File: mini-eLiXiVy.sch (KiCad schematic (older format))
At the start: 175 parts, among them J1 TYPE-C-31-M12_13_EDITED, J2 AVR-ISP-6, SW1 SW_Push, U1 ATmega32U4-AU, U2 WE-TVS-82400102, Y1 Crystal_GND24_Small

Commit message: Added images, adjusted README.md
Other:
- note added: "mini eLiXiVy Schematic, Rev 1a"
- note removed: "mini eLiXiVy Schematic"
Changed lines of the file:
@@
 Text GLabel 7175 1400 1    50   Input ~ 0
 COL13
-Text Notes 2950 750  0    157  ~ 31
-mini eLiXiVy Schematic
+Text Notes 2400 750  0    157  ~ 31
+mini eLiXiVy Schematic, Rev 1a
 $Comp
 L power:GND #PWR0109
@@
 Wire Notes Line
 	7050 6950 7050 8050
-Text Notes 2950 750  0    157  ~ 31
-mini eLiXiVy Schematic
 Text Notes 6670 9892 0    51   ~ 0
 github.com/minibois/eLiXiVy

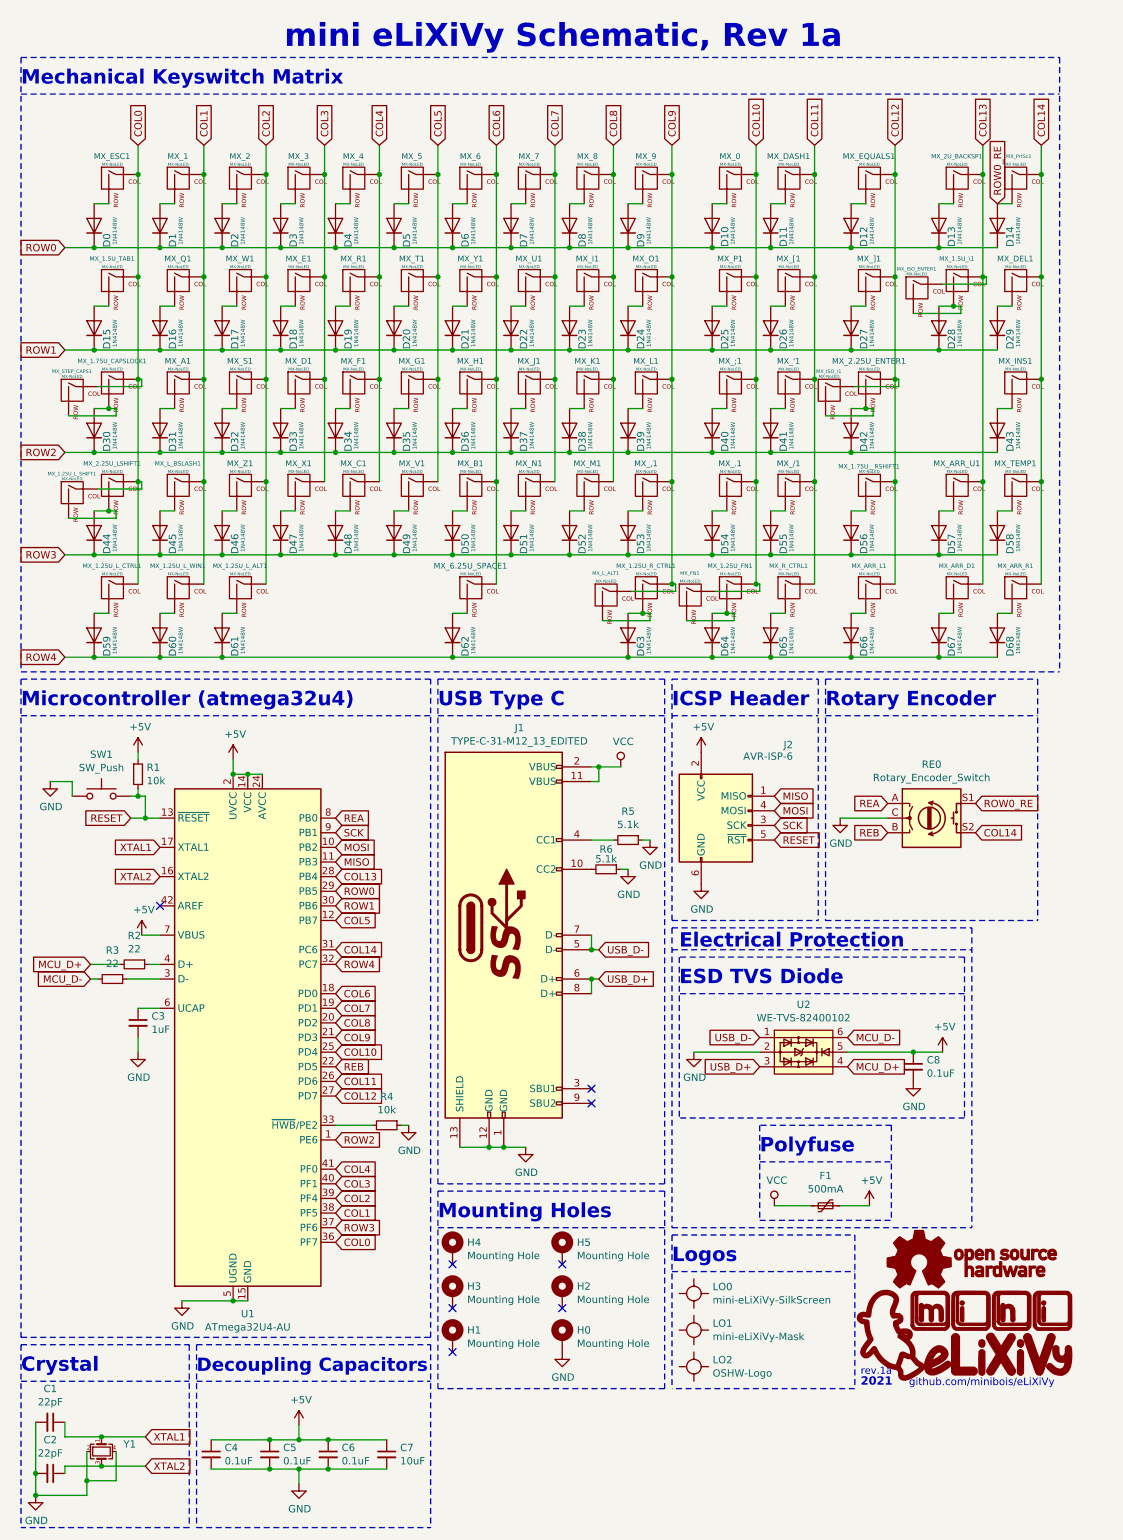
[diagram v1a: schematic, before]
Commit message: rev 1 changes
Changed diode position for D62 and D13 (Spacebar and backspace).
Removed the 'a' from the revision numbers, in the schematic and silkscreen art.
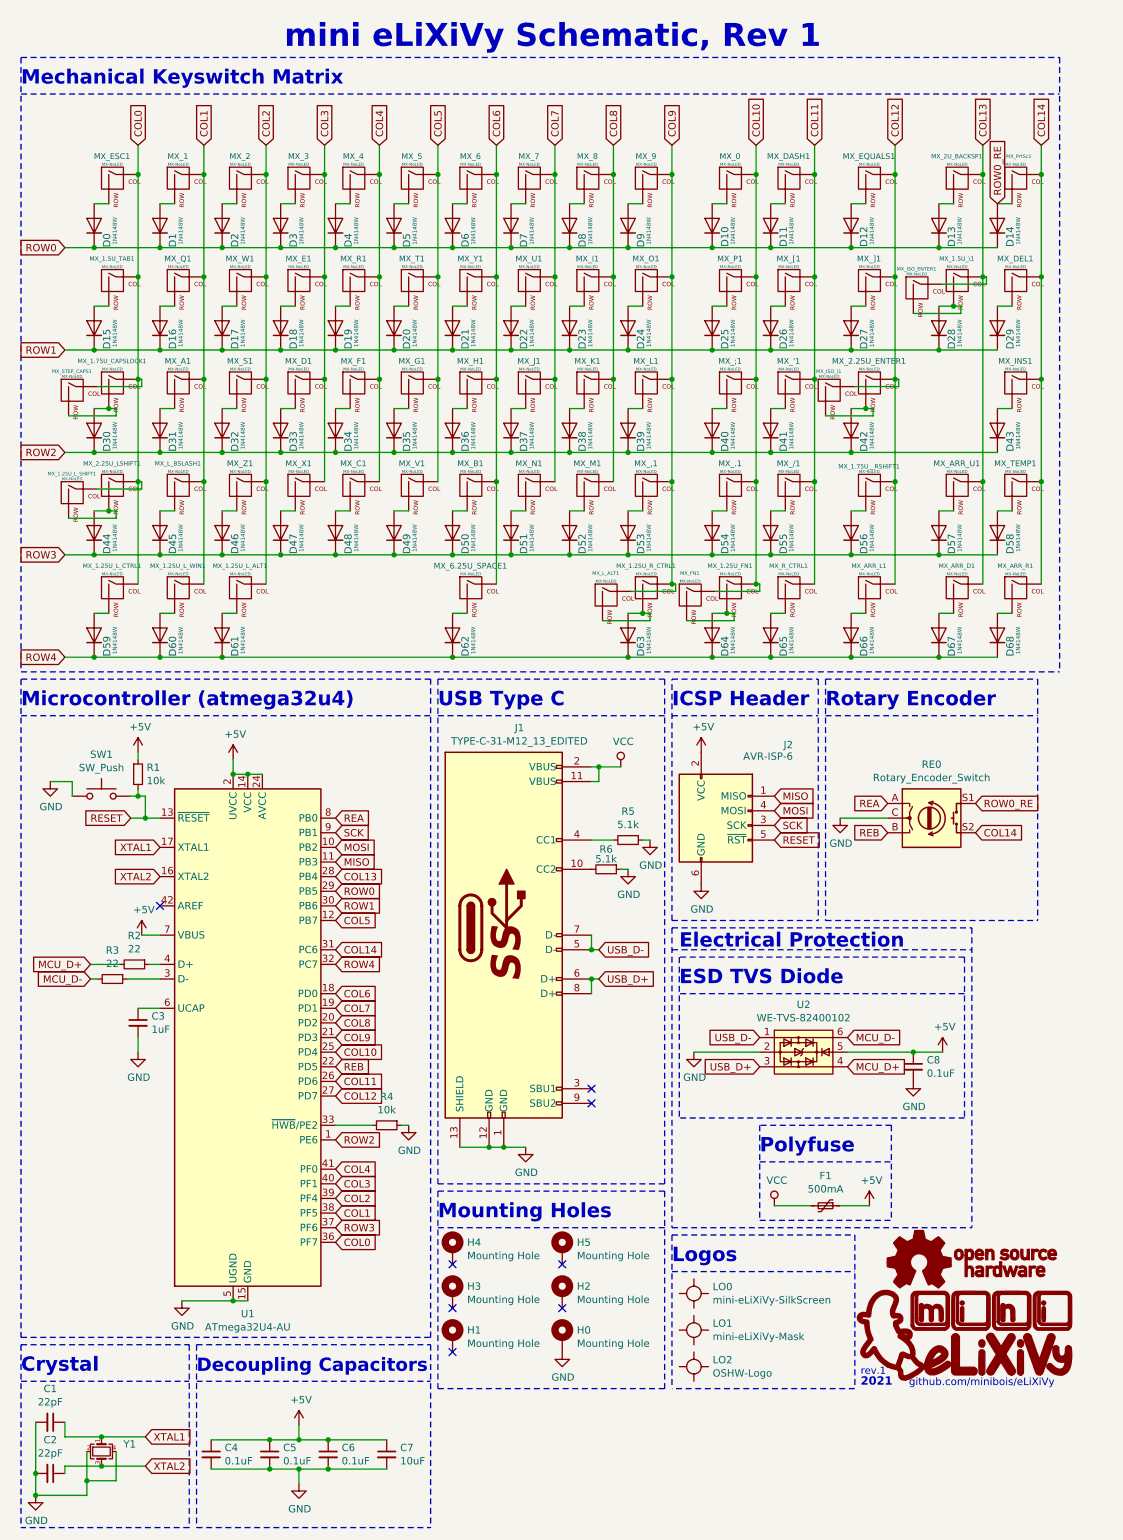
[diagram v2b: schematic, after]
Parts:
- MX_PrtSc1: footprint mini-MX-Tweaks:MXOnly-1U-NoLED-3Pin_tweak -> mini-MX-Tweaks:MXOnly-1U-NoLED_tweak
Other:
- note added: "mini eLiXiVy Schematic, Rev 1"
- note added: "rev.1"
- note removed: "mini eLiXiVy Schematic, Rev 1a"
- note removed: "rev.1a"
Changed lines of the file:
@@
 Sheet 1 1
 Title "eLiXiVy"
-Date "2021-07-09"
-Rev "1a"
+Date "2021-08-05"
+Rev "1"
 Comp "Full License: https://github.com/minibois/eLiXiVy/blob/master/LICENSE.txt"
 Comment1 "of CERN_OHL-S v2 (https://ohwr.org/cern_ohl_s_v2.txt)"
@@
 F 0 "MX_PrtSc1" H 7421 1824 24  0000 C CNN
 F 1 "MX-NoLED" H 7399 1769 20  0000 C CNN
-F 2 "mini-MX-Tweaks:MXOnly-1U-NoLED-3Pin_tweak" H 6800 1625 60  0001 C CNN
+F 2 "mini-MX-Tweaks:MXOnly-1U-NoLED_tweak" H 6800 1625 60  0001 C CNN
 F 3 "" H 6800 1625 60  0001 C CNN
 	1    7425 1650
@@
 COL13
 Text Notes 2400 750  0    157  ~ 31
-mini eLiXiVy Schematic, Rev 1a
+mini eLiXiVy Schematic, Rev 1
 $Comp
 L power:GND #PWR0109
@@
 $EndComp
 Text Notes 6340 9815 0    49   ~ 0
-rev.1a
+rev.1
 Text Notes 6340 9890 0    57   ~ 11
 2021

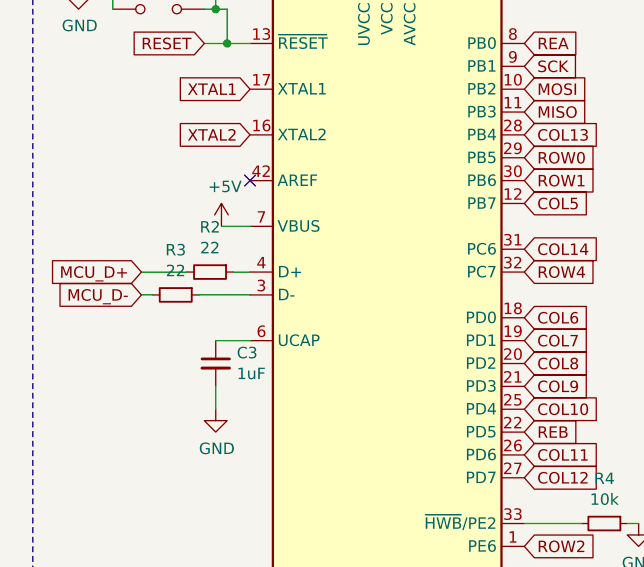
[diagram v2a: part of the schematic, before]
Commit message: Changed R2/R3 location, redid D+/D- traces.
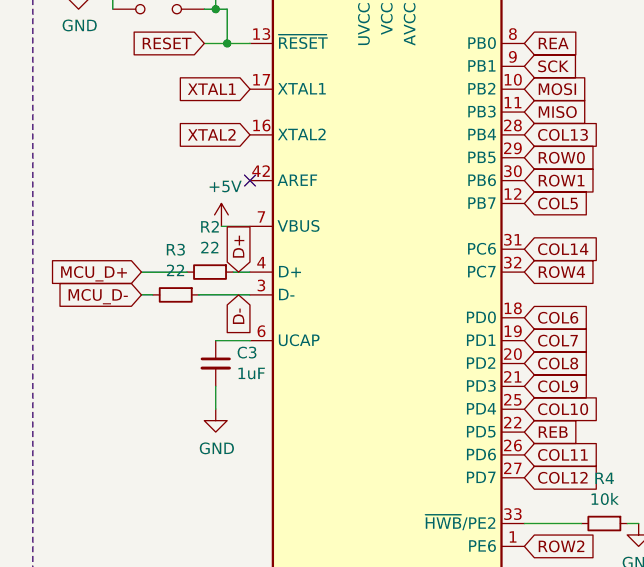
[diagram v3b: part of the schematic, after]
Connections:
- net D-: now reaches R3.1, U1.3 (D-)
- net D+: now reaches R2.1, U1.4 (D+)
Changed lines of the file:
@@
 Wire Wire Line
 	4500 6150 4650 6150
+Text GLabel 1500 7000 1    50   Input ~ 0
+D+
+Text GLabel 1500 7100 3    50   Input ~ 0
+D-
 $EndSCHEMATC

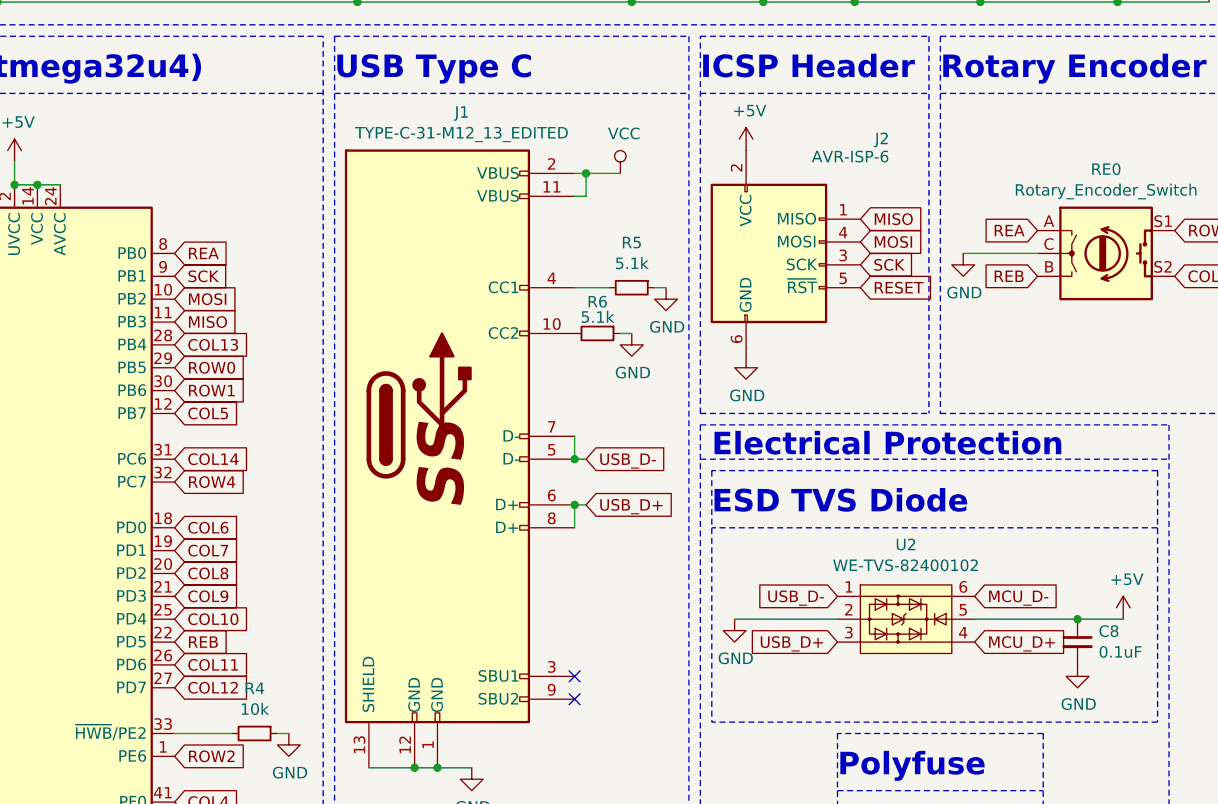
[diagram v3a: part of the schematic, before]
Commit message: Moved R2, R3 and rerouted data line/rotary encoder traces
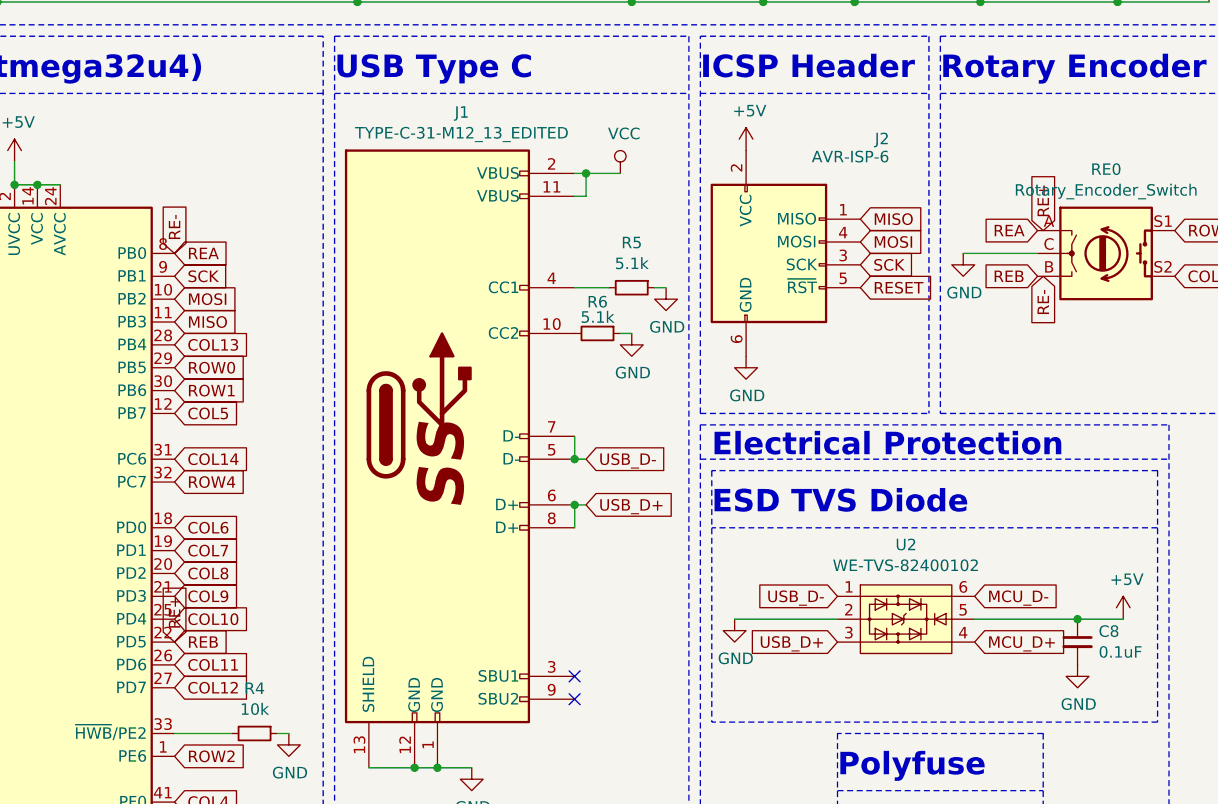
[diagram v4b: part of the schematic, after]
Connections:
- net REA renamed RE-
- net REB renamed RE+
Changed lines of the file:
@@
 	1    0    0    -1
 $EndComp
-Connection ~ 2050 9300
-Wire Wire Line
-	2150 9300 2050 9300
-Wire Wire Line
-	2050 9300 1700 9300
 Text GLabel 1550 6400 0    50   Input ~ 0
 XTAL2
@@
 Text GLabel 2750 6400 2    50   Input ~ 0
 COL13
-$Comp
-L MCU_Microchip_ATmega:ATmega32U4-AU U1
-U 1 1 5F16167A
-P 2150 7500
-F 0 "U1" H 2150 5611 50  0000 C CNN
-F 1 "ATmega32U4-AU" H 2150 5520 50  0000 C CNN
-F 2 "mini-general-tweaks:TQFP-44_10x10mm_P0.8mm_ATmega32U4" H 2150 7500 50  0001 C CIN
-F 3 "http://ww1.microchip.com/downloads/en/DeviceDoc/Atmel-7766-8-bit-AVR-ATmega16U4-32U4_Datasheet.pdf" H 2150 7500 50  0001 C CNN
-	1    2150 7500
-	1    0    0    -1
-$EndComp
 Text GLabel 2750 7000 2    50   Input ~ 0
 ROW4
@@
 Text GLabel 2750 6500 2    50   Input ~ 0
 ROW0
-Connection ~ 2050 5700
-Connection ~ 2150 5700
-Wire Wire Line
-	2250 5700 2150 5700
-Wire Wire Line
-	2150 5700 2050 5700
 Text GLabel 2750 8600 2    50   Input ~ 0
 COL2
@@
 	6200 6000 6525 6000
 Wire Notes Line
-	6100 5050 6100 6700
-Wire Notes Line
 	6100 5050 7550 5050
 Wire Notes Line
@@
 Text GLabel 1500 7100 3    50   Input ~ 0
 D-
+Text GLabel 6550 6100 3    50   Input ~ 0
+RE-
+Text GLabel 6550 5900 1    50   Input ~ 0
+RE+
+Text GLabel 2750 7700 1    50   Input ~ 0
+RE+
+Wire Notes Line
+	6100 5050 6100 6700
+Wire Wire Line
+	2150 5700 2050 5700
+Wire Wire Line
+	2250 5700 2150 5700
+Connection ~ 2150 5700
+Connection ~ 2050 5700
+Wire Wire Line
+	2050 9300 1700 9300
+Wire Wire Line
+	2150 9300 2050 9300
+Connection ~ 2050 9300
+Text GLabel 2750 6000 1    50   Input ~ 0
+RE-
+$Comp
+L MCU_Microchip_ATmega:ATmega32U4-AU U1
+U 1 1 5F16167A
+P 2150 7500
+F 0 "U1" H 2150 5611 50  0000 C CNN
+F 1 "ATmega32U4-AU" H 2150 5520 50  0000 C CNN
+F 2 "mini-general-tweaks:TQFP-44_10x10mm_P0.8mm_ATmega32U4" H 2150 7500 50  0001 C CIN
+F 3 "http://ww1.microchip.com/downloads/en/DeviceDoc/Atmel-7766-8-bit-AVR-ATmega16U4-32U4_Datasheet.pdf" H 2150 7500 50  0001 C CNN
+	1    2150 7500
+	1    0    0    -1
+$EndComp
 $EndSCHEMATC
